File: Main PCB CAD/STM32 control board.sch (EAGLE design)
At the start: 162 parts, among them J1 B3B-PH, J10 B6B-PH, J15 DG301-4P, J16 B10B-PH, J17 B10B-PH, J18 B10B-PH, J19 B10B-PH, J20 B3B-PH, J21 B3B-PH, J22 B3B-PH, J23 B3B-PH, J6 B3B-PH, J7 B3B-PH, J8 B4B-PH, J9 B6B-PH, SW1 B3F-4055, SW2 B3F-4055, SW3 B3F-4055, SW4 B3F-4055, SW5 B3F-4055, U1 STM32G474, U2 TPS7A19, U3 REF3330, U4 REF3318, U5 ICM_20600, U6 DRV8701VIA, U8 L2293Q, X1 CSTNE

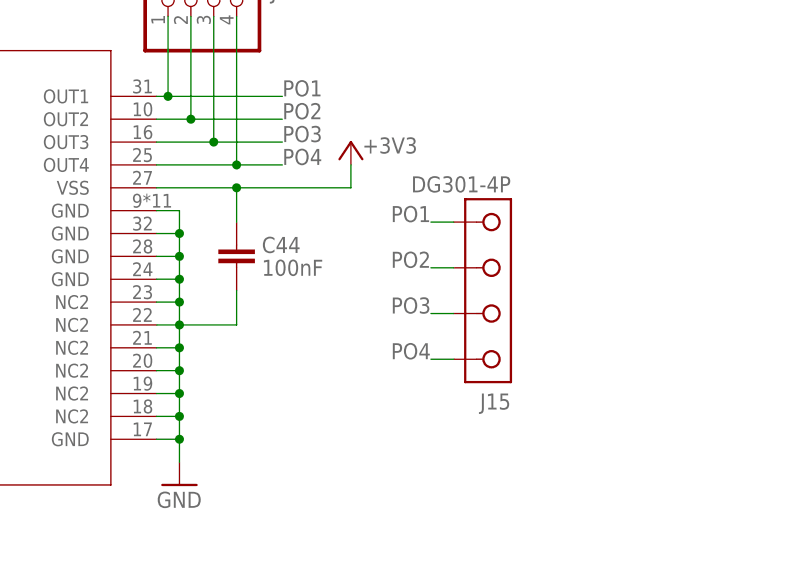
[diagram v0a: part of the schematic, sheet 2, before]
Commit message: screw terminal placement fix
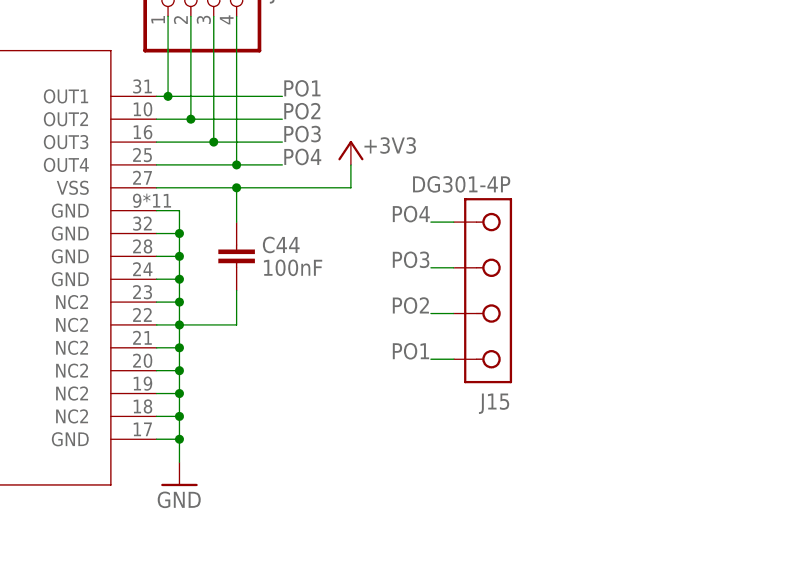
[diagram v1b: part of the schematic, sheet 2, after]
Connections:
- net PO1: now also J15.1; no longer J15.4
- net PO2: now also J15.2; no longer J15.3
- net PO3: now also J15.3; no longer J15.2
- net PO4: now also J15.4; no longer J15.1
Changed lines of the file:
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@@
 </segment>
 <segment>
-<wire x1="275.59" y1="116.84" x2="273.05" y2="116.84" width="0.1524" layer="91" grouprefs="POWER_OUTPUTS"/>
-<label x="273.05" y="116.84" size="1.778" layer="95" rot="MR0" grouprefs="POWER_OUTPUTS"/>
-<pinref part="J15" gate="G$1" pin="2"/>
+<pinref part="J15" gate="G$1" pin="3"/>
+<wire x1="275.59" y1="121.92" x2="273.05" y2="121.92" width="0.1524" layer="91" grouprefs="POWER_OUTPUTS"/>
+<label x="273.05" y="121.92" size="1.778" layer="95" rot="MR0" grouprefs="POWER_OUTPUTS"/>
 </segment>
 </net>
@@
 </segment>
 <segment>
-<pinref part="J15" gate="G$1" pin="3"/>
-<wire x1="275.59" y1="121.92" x2="273.05" y2="121.92" width="0.1524" layer="91" grouprefs="POWER_OUTPUTS"/>
-<label x="273.05" y="121.92" size="1.778" layer="95" rot="MR0" grouprefs="POWER_OUTPUTS"/>
+<wire x1="275.59" y1="116.84" x2="273.05" y2="116.84" width="0.1524" layer="91" grouprefs="POWER_OUTPUTS"/>
+<label x="273.05" y="116.84" size="1.778" layer="95" rot="MR0" grouprefs="POWER_OUTPUTS"/>
+<pinref part="J15" gate="G$1" pin="2"/>
 </segment>
 </net>
@@
 </segment>
 <segment>
-<pinref part="J15" gate="G$1" pin="4"/>
-<wire x1="275.59" y1="127" x2="273.05" y2="127" width="0.1524" layer="91" grouprefs="POWER_OUTPUTS"/>
-<label x="273.05" y="127" size="1.778" layer="95" rot="MR0" grouprefs="POWER_OUTPUTS"/>
+<wire x1="275.59" y1="111.76" x2="273.05" y2="111.76" width="0.1524" layer="91" grouprefs="POWER_OUTPUTS"/>
+<label x="273.05" y="111.76" size="1.778" layer="95" rot="MR0" grouprefs="POWER_OUTPUTS"/>
+<pinref part="J15" gate="G$1" pin="1"/>
 </segment>
 </net>
@@
 </segment>
 <segment>
-<wire x1="275.59" y1="111.76" x2="273.05" y2="111.76" width="0.1524" layer="91" grouprefs="POWER_OUTPUTS"/>
-<label x="273.05" y="111.76" size="1.778" layer="95" rot="MR0" grouprefs="POWER_OUTPUTS"/>
-<pinref part="J15" gate="G$1" pin="1"/>
+<pinref part="J15" gate="G$1" pin="4"/>
+<wire x1="275.59" y1="127" x2="273.05" y2="127" width="0.1524" layer="91" grouprefs="POWER_OUTPUTS"/>
+<label x="273.05" y="127" size="1.778" layer="95" rot="MR0" grouprefs="POWER_OUTPUTS"/>
 </segment>
 </net>

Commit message: routing part 2
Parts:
- added TP1, TP2, TP3: 1.8, testing:TEST_PAD-[1.27MM_SK]
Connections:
- net +3V3: now also TP2.P$1
- net GND: now also TP1.P$1, TP3.P$1
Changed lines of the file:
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@@
 <part name="+3V29" library="supply1" library_urn="urn:adsk.eagle:library:371" deviceset="+3V3" device=""/>
 <part name="J1" library="con-jst-ph" library_urn="urn:adsk.eagle:library:13143856" deviceset="B3B-PH" device="" package3d_urn="urn:adsk.eagle:package:13143941/5"/>
+<part name="TP1" library="testing" library_urn="urn:adsk.eagle:library:13096589" deviceset="TEST_PAD" device="-[1.27MM_SK]" package3d_urn="urn:adsk.eagle:package:15234684/3" value="1.8"/>
+<part name="TP2" library="testing" library_urn="urn:adsk.eagle:library:13096589" deviceset="TEST_PAD" device="-[1.27MM_SK]" package3d_urn="urn:adsk.eagle:package:15234684/3" value="1.8"/>
+<part name="TP3" library="testing" library_urn="urn:adsk.eagle:library:13096589" deviceset="TEST_PAD" device="-[1.27MM_SK]" package3d_urn="urn:adsk.eagle:package:15234684/3" value="1.8"/>
 </parts>
 <sheets>
@@
 <instance part="J1" gate="G$1" x="30.48" y="204.47" smashed="yes">
 <attribute name="VALUE" x="29.21" y="196.85" size="1.778" layer="95"/>
+</instance>
+<instance part="TP1" gate="G$1" x="96.52" y="158.75" smashed="yes" rot="R270">
+<attribute name="NAME" x="96.52" y="156.21" size="1.27" layer="95" align="center-left"/>
+</instance>
+<instance part="TP2" gate="G$1" x="123.19" y="250.19" smashed="yes" rot="R90">
+<attribute name="NAME" x="123.19" y="252.73" size="1.27" layer="95" rot="R180" align="center-left"/>
+</instance>
+<instance part="TP3" gate="G$1" x="123.19" y="208.28" smashed="yes" rot="R270">
+<attribute name="NAME" x="123.19" y="205.74" size="1.27" layer="95" align="center-left"/>
 </instance>
 </instances>
@@
 <wire x1="76.2" y1="166.37" x2="76.2" y2="163.83" width="0.1524" layer="91" grouprefs="POWER_STAGE"/>
 <pinref part="U4" gate="A" pin="GND"/>
-<wire x1="76.2" y1="163.83" x2="106.68" y2="163.83" width="0.1524" layer="91" grouprefs="POWER_STAGE"/>
+<wire x1="76.2" y1="163.83" x2="96.52" y2="163.83" width="0.1524" layer="91" grouprefs="POWER_STAGE"/>
+<wire x1="96.52" y1="163.83" x2="106.68" y2="163.83" width="0.1524" layer="91" grouprefs="POWER_STAGE"/>
 <wire x1="106.68" y1="163.83" x2="106.68" y2="175.26" width="0.1524" layer="91" grouprefs="POWER_STAGE"/>
 <wire x1="106.68" y1="175.26" x2="105.41" y2="175.26" width="0.1524" layer="91" grouprefs="POWER_STAGE"/>
@@
 <wire x1="106.68" y1="163.83" x2="106.68" y2="161.29" width="0.1524" layer="91" grouprefs="POWER_STAGE"/>
 <pinref part="GND3" gate="1" pin="GND"/>
+<pinref part="TP1" gate="G$1" pin="P$1"/>
+<wire x1="96.52" y1="161.29" x2="96.52" y2="163.83" width="0.1524" layer="91"/>
+<junction x="96.52" y="163.83"/>
 </segment>
 <segment>
@@
 <pinref part="NEG" gate="1" pin="P"/>
 <wire x1="27.94" y1="226.06" x2="19.05" y2="226.06" width="0.1524" layer="91" grouprefs="POWER_STAGE"/>
+<pinref part="TP3" gate="G$1" pin="P$1"/>
+<wire x1="123.19" y1="210.82" x2="123.19" y2="214.63" width="0.1524" layer="91"/>
+<wire x1="123.19" y1="214.63" x2="111.76" y2="214.63" width="0.1524" layer="91"/>
+<junction x="111.76" y="214.63"/>
 </segment>
 <segment>
@@
 <segment>
 <pinref part="U2" gate="A" pin="VOUT"/>
-<wire x1="111.76" y1="248.92" x2="111.76" y2="240.03" width="0.1524" layer="91" grouprefs="POWER_STAGE"/>
+<wire x1="111.76" y1="248.92" x2="111.76" y2="242.57" width="0.1524" layer="91" grouprefs="POWER_STAGE"/>
+<wire x1="111.76" y1="242.57" x2="111.76" y2="240.03" width="0.1524" layer="91" grouprefs="POWER_STAGE"/>
 <wire x1="111.76" y1="240.03" x2="111.76" y2="234.95" width="0.1524" layer="91" grouprefs="POWER_STAGE"/>
 <wire x1="111.76" y1="234.95" x2="111.76" y2="231.14" width="0.1524" layer="91" grouprefs="POWER_STAGE"/>
@@
 <wire x1="134.62" y1="234.95" x2="123.19" y2="234.95" width="0.1524" layer="91" grouprefs="POWER_STAGE"/>
 <junction x="123.19" y="234.95" grouprefs="POWER_STAGE"/>
-</segment>
-<segment>
+<pinref part="TP2" gate="G$1" pin="P$1"/>
+<wire x1="123.19" y1="247.65" x2="123.19" y2="242.57" width="0.1524" layer="91"/>
+<wire x1="123.19" y1="242.57" x2="111.76" y2="242.57" width="0.1524" layer="91"/>
+<junction x="111.76" y="242.57"/>
+</segment>
+<segment>

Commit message: routing part 3
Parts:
- R5, R6, R7, R8: device Resistors:POTEMTIOMETER_EU -> Resistors:POTEMTIOMETER_EULONG
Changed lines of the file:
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@@
 <part name="+3V1" library="supply1" library_urn="urn:adsk.eagle:library:371" deviceset="+3V3" device=""/>
 <part name="+3V10" library="supply1" library_urn="urn:adsk.eagle:library:371" deviceset="+3V3" device=""/>
-<part name="SW1" library="buttons and switches" library_urn="urn:adsk.eagle:library:14616530" deviceset="B3F-4055" device="" package3d_urn="urn:adsk.eagle:package:17006412/3"/>
+<part name="SW1" library="buttons and switches" library_urn="urn:adsk.eagle:library:14616530" deviceset="B3F-4055" device="" package3d_urn="urn:adsk.eagle:package:17006412/4"/>
 <part name="GND20" library="supply1" library_urn="urn:adsk.eagle:library:371" deviceset="GND" device=""/>
 <part name="C5" library="Capacitors" library_urn="urn:adsk.eagle:library:13360199" deviceset="C-EU-CERAMIC" device="0402" package3d_urn="urn:adsk.eagle:package:13360227/6" value="100nF"/>
@@
 <part name="GND24" library="supply1" library_urn="urn:adsk.eagle:library:371" deviceset="GND" device=""/>
 <part name="GND25" library="supply1" library_urn="urn:adsk.eagle:library:371" deviceset="GND" device=""/>
-<part name="SW2" library="buttons and switches" library_urn="urn:adsk.eagle:library:14616530" deviceset="B3F-4055" device="" package3d_urn="urn:adsk.eagle:package:17006412/3"/>
-<part name="SW3" library="buttons and switches" library_urn="urn:adsk.eagle:library:14616530" deviceset="B3F-4055" device="" package3d_urn="urn:adsk.eagle:package:17006412/3"/>
-<part name="SW4" library="buttons and switches" library_urn="urn:adsk.eagle:library:14616530" deviceset="B3F-4055" device="" package3d_urn="urn:adsk.eagle:package:17006412/3"/>
+<part name="SW2" library="buttons and switches" library_urn="urn:adsk.eagle:library:14616530" deviceset="B3F-4055" device="" package3d_urn="urn:adsk.eagle:package:17006412/4"/>
+<part name="SW3" library="buttons and switches" library_urn="urn:adsk.eagle:library:14616530" deviceset="B3F-4055" device="" package3d_urn="urn:adsk.eagle:package:17006412/4"/>
+<part name="SW4" library="buttons and switches" library_urn="urn:adsk.eagle:library:14616530" deviceset="B3F-4055" device="" package3d_urn="urn:adsk.eagle:package:17006412/4"/>
 <part name="C24" library="Capacitors" library_urn="urn:adsk.eagle:library:13360199" deviceset="C-EU-CERAMIC" device="0402" package3d_urn="urn:adsk.eagle:package:13360227/6" value="100nF"/>
 <part name="C25" library="Capacitors" library_urn="urn:adsk.eagle:library:13360199" deviceset="C-EU-CERAMIC" device="0402" package3d_urn="urn:adsk.eagle:package:13360227/6" value="100nF"/>
@@
 <part name="+3V24" library="supply1" library_urn="urn:adsk.eagle:library:371" deviceset="+3V3" device=""/>
 <part name="GND29" library="supply1" library_urn="urn:adsk.eagle:library:371" deviceset="GND" device=""/>
-<part name="R5" library="Resistors" library_urn="urn:adsk.eagle:library:13360588" deviceset="POTEMTIOMETER_EU" device="" package3d_urn="urn:adsk.eagle:package:17016698/4" value="10K"/>
-<part name="R6" library="Resistors" library_urn="urn:adsk.eagle:library:13360588" deviceset="POTEMTIOMETER_EU" device="" package3d_urn="urn:adsk.eagle:package:17016698/4" value="10K"/>
-<part name="R7" library="Resistors" library_urn="urn:adsk.eagle:library:13360588" deviceset="POTEMTIOMETER_EU" device="" package3d_urn="urn:adsk.eagle:package:17016698/4" value="10K"/>
+<part name="R5" library="Resistors" library_urn="urn:adsk.eagle:library:13360588" deviceset="POTEMTIOMETER_EU" device="LONG" package3d_urn="urn:adsk.eagle:package:22300933/2" value="10K"/>
+<part name="R6" library="Resistors" library_urn="urn:adsk.eagle:library:13360588" deviceset="POTEMTIOMETER_EU" device="LONG" package3d_urn="urn:adsk.eagle:package:22300933/2" value="10K"/>
+<part name="R7" library="Resistors" library_urn="urn:adsk.eagle:library:13360588" deviceset="POTEMTIOMETER_EU" device="LONG" package3d_urn="urn:adsk.eagle:package:22300933/2" value="10K"/>
 <part name="GND31" library="supply1" library_urn="urn:adsk.eagle:library:371" deviceset="GND" device=""/>
 <part name="+3V25" library="Hople_supply" library_urn="urn:adsk.eagle:library:16851455" deviceset="+3V" device=""/>
-<part name="R8" library="Resistors" library_urn="urn:adsk.eagle:library:13360588" deviceset="POTEMTIOMETER_EU" device="" package3d_urn="urn:adsk.eagle:package:17016698/4" value="10K"/>
-<part name="SW5" library="buttons and switches" library_urn="urn:adsk.eagle:library:14616530" deviceset="B3F-4055" device="" package3d_urn="urn:adsk.eagle:package:17006412/3"/>
+<part name="R8" library="Resistors" library_urn="urn:adsk.eagle:library:13360588" deviceset="POTEMTIOMETER_EU" device="LONG" package3d_urn="urn:adsk.eagle:package:22300933/2" value="10K"/>
+<part name="SW5" library="buttons and switches" library_urn="urn:adsk.eagle:library:14616530" deviceset="B3F-4055" device="" package3d_urn="urn:adsk.eagle:package:17006412/4"/>
 <part name="C27" library="Capacitors" library_urn="urn:adsk.eagle:library:13360199" deviceset="C-EU-CERAMIC" device="0402" package3d_urn="urn:adsk.eagle:package:13360227/6" value="100nF"/>
 <part name="R12" library="Resistors" library_urn="urn:adsk.eagle:library:13360588" deviceset="R-EU" device="0402" package3d_urn="urn:adsk.eagle:package:15234387/3" value="10k"/>

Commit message: for routing rewiew
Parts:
- removed D34, D35, D36, D37: Blue, Semiconductor_devices:LED0805
- removed J16, J17, J18, J19: B10B-PH, con-jst-ph:B10B-PH
- removed J20: B3B-PH, con-jst-ph:B3B-PH
- removed RM9: RES_ARRAY0603, Resistors:RES_ARRAY0603
- added D2, D3, D4, D5: Blue, Semiconductor_devices:LED0805
- added J14, J4: B6B-PH, con-jst-ph:B6B-PH
- added J2, J5: B3B-PH, con-jst-ph:B3B-PH
- added J3: B4B-PH, con-jst-ph:B4B-PH
- added RM1: RES_ARRAY0603, Resistors:RES_ARRAY0603
- J10: value B6B-PH -> B3B-PH; device con-jst-ph:B6B-PH -> con-jst-ph:B3B-PH
- J6, J7: value B3B-PH -> B10B-PH; device con-jst-ph:B3B-PH -> con-jst-ph:B10B-PH
- J8: value B4B-PH -> B10B-PH; device con-jst-ph:B4B-PH -> con-jst-ph:B10B-PH
- J9: value B6B-PH -> B10B-PH; device con-jst-ph:B6B-PH -> con-jst-ph:B10B-PH
- JP1: device commonly used connectors:PINHD-1X4 -> commonly used connectors:PINHD-1X3
- JP3: device commonly used connectors:PINHD-1X6-OCT -> commonly used connectors:PINHD-1X3
- JP8: device commonly used connectors:PINHD-1X3 -> commonly used connectors:PINHD-1X6-OCT
- JP9: device commonly used connectors:PINHD-1X3 -> commonly used connectors:PINHD-1X4
- renumbered GND_ to $1_148_$_2020-08-01_13-42-32, J21 to J11, J22 to J12, J23 to J13, NEG to PAD2, POS to PAD1
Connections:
- net +3V: now also J10.1, JP5.1, JP6.1; no longer J20.1, JP8.1, JP9.1
- net +3V3: now also J14.2, J3.1, J4.1, J6.1, J7.1, JP2.1, JP8.2; no longer J10.2, J16.1, J17.1, J18.1, J19.1, JP2.2, JP3.1
- net ENCODER_1: now also J14.3, JP8.3; no longer J10.3, JP2.3
- net ENCODER_2: now also J14.4, JP8.4; no longer J10.4, JP2.4
- net GND: now also J10.3, J14.5, J2.3, J3.4, J4.6, J5.3, J6.2, J7.2, J8.2, J9.2, JP1.3, JP2.6, JP3.3, JP8.5, RM1_1.1, RM1_2.1, RM1_3.1, RM1_4.1; no longer J10.5, J16.2, J17.2, J18.2, J19.2, J20.3, J6.3, J7.3, J8.4, J9.6, JP2.5, JP3.6, JP8.3, JP9.3, RM9_1.1, RM9_2.1, RM9_3.1, RM9_4.1
- net I2C3_SCL: now also J5.2, JP3.2; no longer J6.2, JP5.2
- net I2C3_SDA: now also J5.1, JP3.1; no longer J6.1, JP5.1
- net M2: now also J14.6, JP8.6; no longer J10.6, JP2.6
- net M_SH1: now also J14.1, JP8.1; no longer J10.1, JP2.1
- net N$10: now also D4.C, RM1_2.2; no longer D28.C, RM4_2.2
- net N$11: now also D6.C, RM1_3.2; no longer D29.C, RM4_3.2
- net N$12: now also D8.C, RM1_4.2; no longer D30.C, RM4_4.2
- net N$23: now also D18.C, RM5_1.2; no longer D35.C, RM2_1.2
- net N$25: now also D20.C, RM5_2.2; no longer D36.C, RM2_2.2
- net N$26: now also D22.C, RM5_3.2; no longer D14.C, RM2_3.2
- net N$27: now also D24.C, RM5_4.2; no longer D15.C, RM2_4.2
- net N$28: now also D26.C, RM7_1.2; no longer D24.C, RM3_1.2
- net N$29: now also D28.C, RM7_2.2; no longer D25.C, RM3_2.2
- net N$3: now also D16.C, RM3_4.2; no longer D34.C, RM5_4.2
- net N$30: now also D30.C, RM7_3.2; no longer D26.C, RM3_3.2
- net N$31: now also D32.C, RM7_4.2; no longer D37.C, RM3_4.2
- net N$34: now also D3.C, RM2_1.2; no longer D6.C, RM6_1.2
- net N$35: now also D5.C, RM2_2.2; no longer D10.C, RM6_2.2
- net N$36: now also RM2_3.2; no longer RM6_3.2
- net N$38: now also D9.C, RM2_4.2; no longer D11.C, RM6_4.2
- net N$39: now also D11.C, RM4_1.2; no longer D8.C, RM7_1.2
- net N$4: now also D14.C, RM3_3.2; no longer D33.C, RM5_3.2
- net N$40: now also D13.C, RM4_2.2; no longer D12.C, RM7_2.2
- net N$41: now also D15.C, RM4_3.2; no longer D9.C, RM7_3.2
- net N$42: now also D17.C, RM4_4.2; no longer D13.C, RM7_4.2
- net N$43: now also D19.C, RM6_1.2; no longer D16.C, RM8_1.2
- net N$44: now also D21.C, RM6_2.2; no longer D20.C, RM8_2.2
- net N$45: now also D23.C, RM6_3.2; no longer D17.C, RM8_3.2
- net N$46: now also D25.C, RM6_4.2; no longer D21.C, RM8_4.2
- net N$47: now also D27.C, RM8_1.2; no longer D18.C, RM9_1.2
- net N$48: now also D29.C, RM8_2.2; no longer D22.C, RM9_2.2
- net N$49: now also D31.C, RM8_3.2; no longer D19.C, RM9_3.2
- net N$5: now also D12.C, RM3_2.2; no longer D32.C, RM5_2.2
- net N$50: now also D33.C, RM8_4.2; no longer D23.C, RM9_4.2
- net N$6: now also D10.C, RM3_1.2; no longer D31.C, RM5_1.2
- net N$9: now also D2.C, RM1_1.2; no longer D27.C, RM4_1.2
- net PA0: now also J10.2, JP4.2; no longer J20.2, JP9.2
- net PA1: now also JP5.2; no longer JP8.2
- net PA2: now also JP6.2; no longer JP7.2
- net PA3: now also JP7.2; no longer JP4.2
- net PD0: now also D2.A, J6.3; no longer D27.A, J19.3
- net PD1: now also D4.A, J6.4; no longer D28.A, J19.4
- net PD10: now also D22.A, J7.5; no longer D14.A, J16.5
- net PD11: now also D24.A, J7.6; no longer D15.A, J16.6
- net PD12: now also D26.A, J7.7; no longer D24.A, J16.7
- net PD13: now also D28.A, J7.8; no longer D25.A, J16.8
- net PD14: now also D30.A, J7.9; no longer D26.A, J16.9
- net PD15: now also D32.A, J7.10; no longer D37.A, J16.10
- net PD2: now also D6.A, J6.5; no longer D29.A, J19.5
- net PD3: now also D8.A, J6.6; no longer D30.A, J19.6
- net PD4: now also D10.A, J6.7; no longer D31.A, J19.7
- net PD5: now also D12.A, J6.8; no longer D32.A, J19.8
- net PD6: now also D14.A, J6.9; no longer D33.A, J19.9
- net PD7: now also D16.A, J6.10; no longer D34.A, J19.10
- net PD8: now also D18.A, J7.3; no longer D35.A, J16.3
- net PD9: now also D20.A, J7.4; no longer D36.A, J16.4
- net PE0: now also D3.A, J8.3; no longer D6.A, J17.3
- net PE1: now also D5.A, J8.4; no longer D10.A, J17.4
- net PE10: now also D23.A, J9.5; no longer D17.A, J18.5
- net PE11: now also D25.A, J9.6; no longer D21.A, J18.6
- net PE12: now also D27.A, J9.7; no longer D18.A, J18.7
- net PE13: now also D29.A, J9.8; no longer D22.A, J18.8
- net PE14: now also D31.A, J9.9; no longer D19.A, J18.9
- net PE15: now also D33.A, J9.10; no longer D23.A, J18.10
- net PE2: now also J8.5; no longer J17.5
- net PE3: now also D9.A, J8.6; no longer D11.A, J17.6
- net PE4: now also D11.A, J8.7; no longer D8.A, J17.7
- net PE5: now also D13.A, J8.8; no longer D12.A, J17.8
- net PE6: now also D15.A, J8.9; no longer D9.A, J17.9
- net PE7: now also D17.A, J8.10; no longer D13.A, J17.10
- net PE8: now also D19.A, J9.3; no longer D16.A, J18.3
- net PE9: now also D21.A, J9.4; no longer D20.A, J18.4
- net PO1: now also JP9.1; no longer JP1.1
- net PO2: now also JP9.2; no longer JP1.2
- net PO3: now also JP9.3; no longer JP1.3
- net PO4: now also JP9.4; no longer JP1.4
- net SPI3_MISO: now also J4.3, JP2.3; no longer J9.3, JP3.3
- net SPI3_MOSI: now also J4.2, JP2.2; no longer J9.2, JP3.2
- net SPI3_SCK: now also J4.4, JP2.4; no longer J9.4, JP3.4
- net SPI_CS: now also J4.5, JP2.5; no longer J9.5, JP3.5
- net SWCLK: now also J3.3; no longer J8.3
- net SWDIO: now also J3.2; no longer J8.2
- net USART3_RX: now also J2.2, JP1.2; no longer J7.2, JP6.2
- net USART3_TX: now also J2.1, JP1.1; no longer J7.1, JP6.1
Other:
- moved on the sheet: D10, D11, D12, D13, D14, D15, D16, D17, D18, D19, D20, D21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
